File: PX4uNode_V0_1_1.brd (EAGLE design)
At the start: 45.4 x 34 mm, 129 parts, among them M3_MOUNT1101 MOUNT-HOLE3.1MM, M3_MOUNT1102 MOUNT-HOLE3.1MM, M3_MOUNT1103 MOUNT-HOLE3.1MM, M3_MOUNT1104 MOUNT-HOLE3.1MM, U101 STM32F4X7VX, U401 MAX3051, U402 MAX3051, X101 3.2x2.5 mm / 24 MHz / 15 ppm

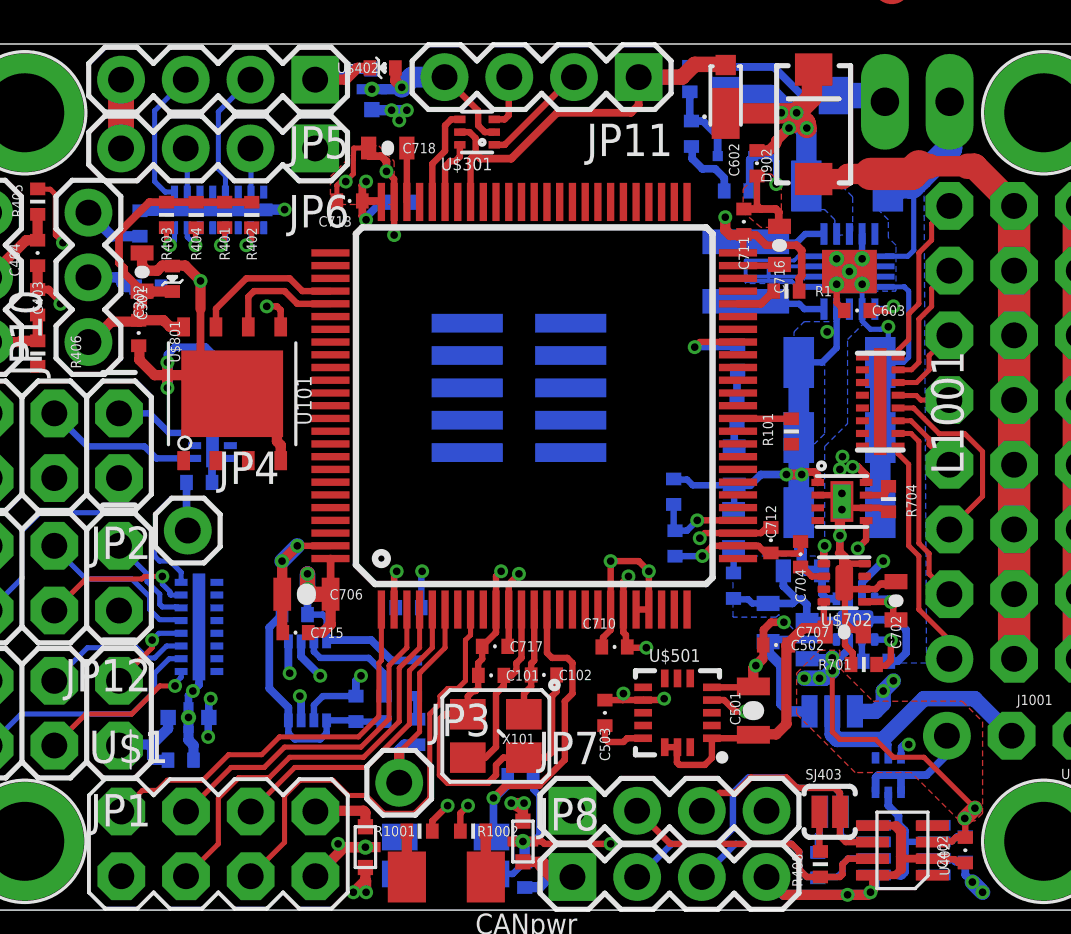
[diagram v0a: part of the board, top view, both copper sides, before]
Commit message: Battery added.  Floods added to power tracks
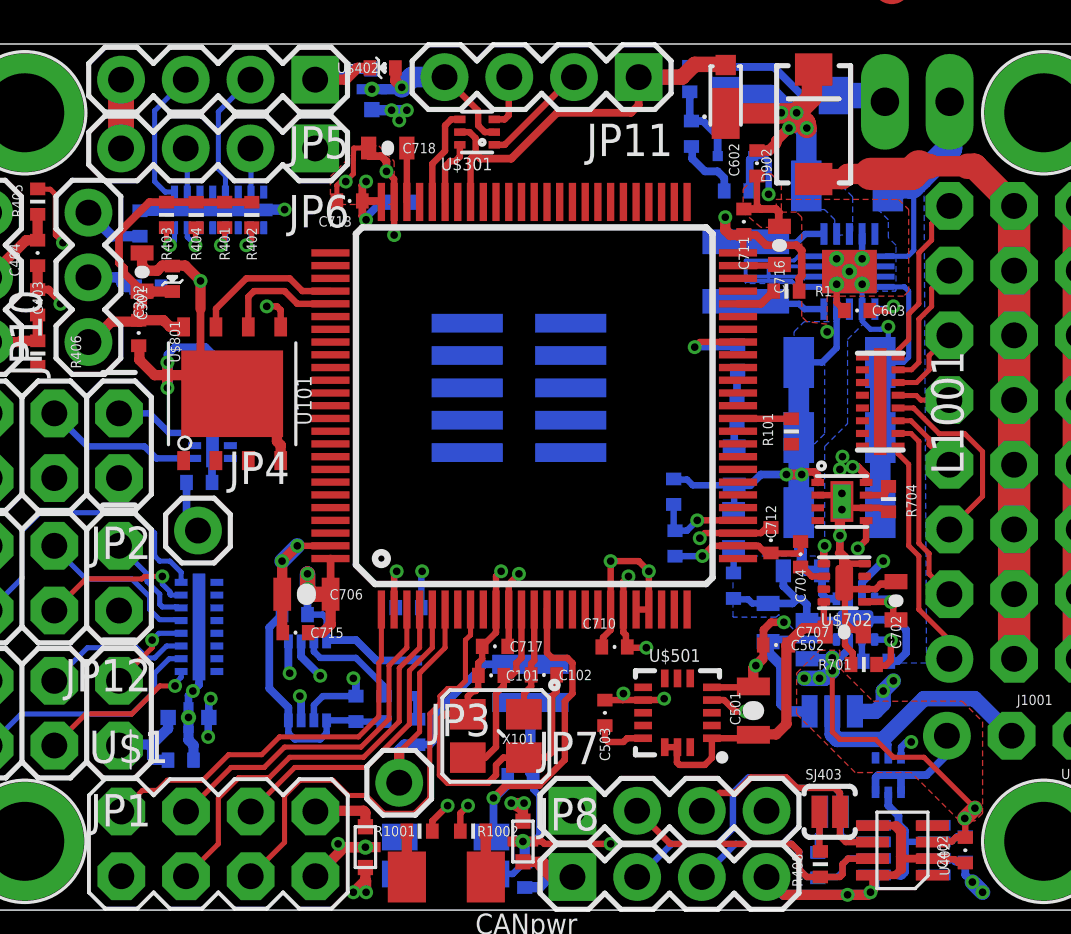
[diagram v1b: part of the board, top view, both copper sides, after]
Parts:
- added U$4: MS621FE, pixhawk2:MS621FE
- moved JP4 0.40 mm to (22.3, 19.1)
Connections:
- net GND: now also U$4.2
- net VBAT: now also U$4.1
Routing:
- net VBAT: track 9.65 -> 16.0 mm
- net GND: track 233.2 -> 236.3 mm
- added copper zone on layer 15, net 5V_S3_FILTERED
- added copper zone on layer 15, net VDD_5V_PERIPH

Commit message: Almost routed
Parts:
- moved R101 0.40 mm to (45.6, 22.6)
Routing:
- net FMU-CH8: track 0.97 -> 47.3 mm, vias 1 -> 7
- net CAN1_TX: track 0.00 -> 45.7 mm, vias 0 -> 3
- net FMU_AUX_ADC1: track 2.80 -> 47.7 mm, vias 1 -> 6
- net CAN1_RX: track 0.00 -> 44.5 mm, vias 0 -> 6
- net SPEKTRUM_RX: track 0.91 -> 40.3 mm, vias 1 -> 6
- net CAN2_TX: track 0.00 -> 38.7 mm, vias 0 -> 6
- net FMU-USART3_RTS: track 0.00 -> 37.7 mm, vias 0 -> 3
- net CAN2_RX: track 0.00 -> 37.6 mm, vias 0 -> 4
- net FMU-USART3_RX: track 0.00 -> 36.1 mm, vias 0 -> 5
- net !VDD_5V_PERIPH_EN: track 1.23 -> 37.1 mm, vias 1 -> 6
- net FMU-USART3_CTS: track 0.00 -> 34.9 mm, vias 0 -> 6
- net ACCEL_DRDY: track 0.00 -> 34.1 mm, vias 0 -> 2
- net FMU_AUX_ADC2: track 0.00 -> 31.3 mm, vias 0 -> 2
- net FMU-LED_SAFETY: track 0.00 -> 30.4 mm, vias 0 -> 4
- net FMU-USART3_TX: track 0.00 -> 30.3 mm, vias 0 -> 5
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
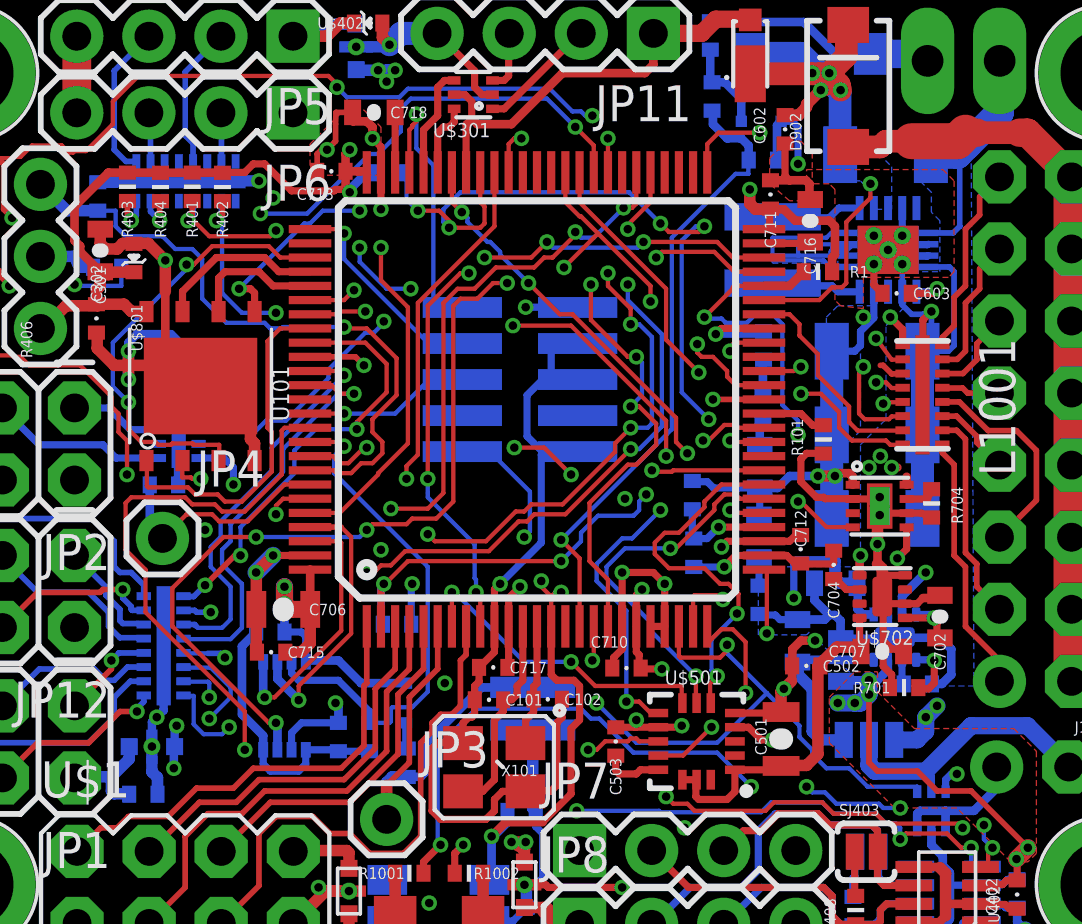
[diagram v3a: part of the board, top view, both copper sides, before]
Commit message: Servo output channels ripped up for reshuffle
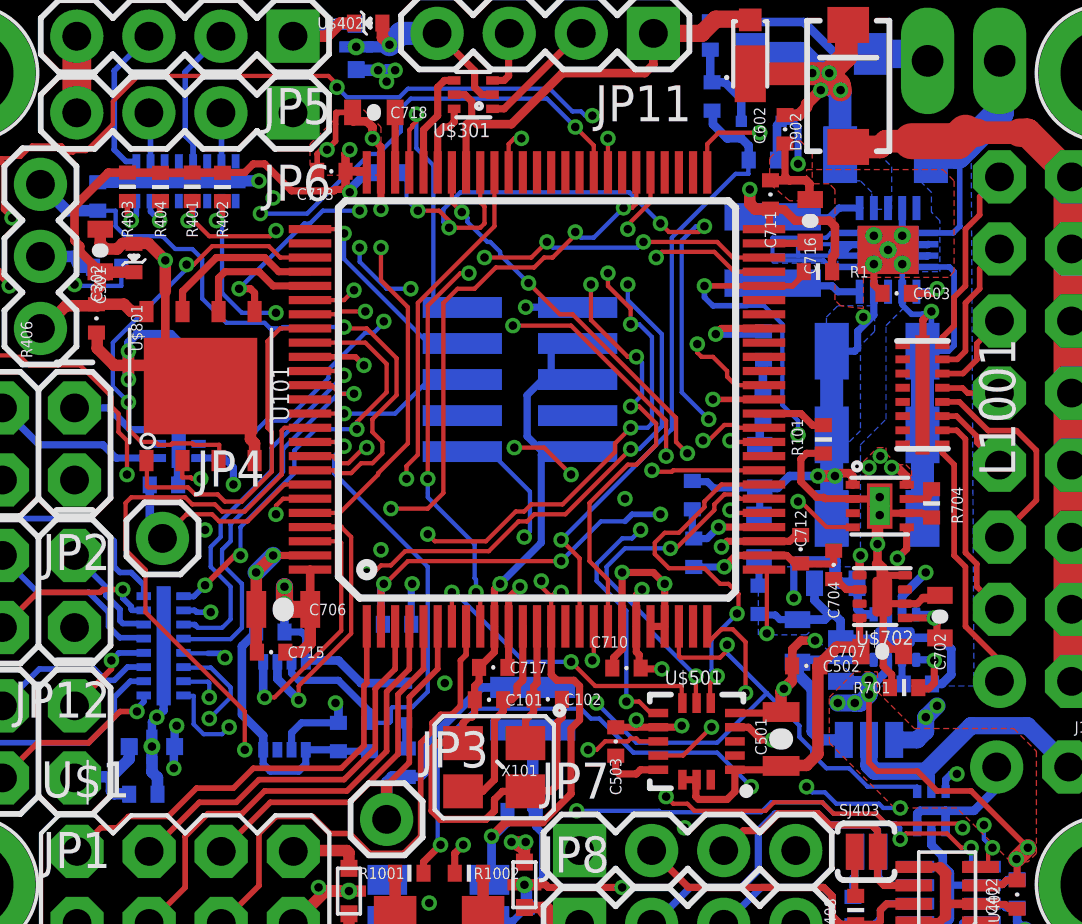
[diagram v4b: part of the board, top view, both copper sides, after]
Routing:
- net FMU-CH8: track 47.3 -> 0.04 mm, vias 7 -> 0
- net FMU-CH1: track 20.1 -> 0.00 mm, vias 2 -> 0
- net FMU-CH5: track 17.0 -> 0.00 mm, vias 2 -> 0
- net FMU-CH7: track 15.7 -> 0.00 mm, vias 2 -> 0
- net FMU-CH3: track 9.97 -> 0.00 mm, vias 2 -> 0
- net FMU-CH2: track 7.58 -> 0.00 mm
- net FMU-CH4: track 7.10 -> 0.21 mm, vias 2 -> 0
- net SPI_INT_SCK: track 16.4 -> 12.1 mm
- net FMU-CH6: track 0.91 -> 0.00 mm
- added copper zone on layer 1, net VDD_5V_PERIPH

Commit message: Layout done
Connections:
- net FMU-CH1: now also L1001.P$4; no longer L1001.P$8
- net FMU-CH2: now also L1001.P$5; no longer L1001.P$7
- net FMU-CH3: now also L1001.P$6; no longer L1001.P$5
- net FMU-CH4: now also L1001.P$7; no longer L1001.P$6
- net FMU-CH5: now also L1001.P$2; no longer L1001.P$4
- net FMU-CH7: now also L1001.P$8; no longer L1001.P$2
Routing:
- net FMU-CH8: track 0.04 -> 42.0 mm, vias 0 -> 5
- net FMU-CH6: track 0.00 -> 21.4 mm, vias 0 -> 3
- net FMU-CH7: track 0.00 -> 15.7 mm, vias 0 -> 2
- net FMU-CH5: track 0.00 -> 15.3 mm, vias 0 -> 2
- net FMU-CH1: track 0.00 -> 6.63 mm
- net FMU-CH2: track 0.00 -> 6.46 mm
- net FMU-CH3: track 0.00 -> 6.00 mm
- net FMU-CH4: track 0.21 -> 5.96 mm
- net VDD_5V_PERIPH: track 86.8 -> 91.3 mm
- net CAN1_RX: track 44.5 -> 46.3 mm
- net FMU-USART3_CTS: track 34.9 -> 33.9 mm, vias 6 -> 4
- net !GYRO_CS: track 11.3 -> 12.2 mm
- net SPEKTRUM_RX: track 40.3 -> 41.2 mm
- net MAG_DRDY: track 15.6 -> 16.3 mm
- net !VDD_5V_PERIPH_OC: track 16.1 -> 16.8 mm
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
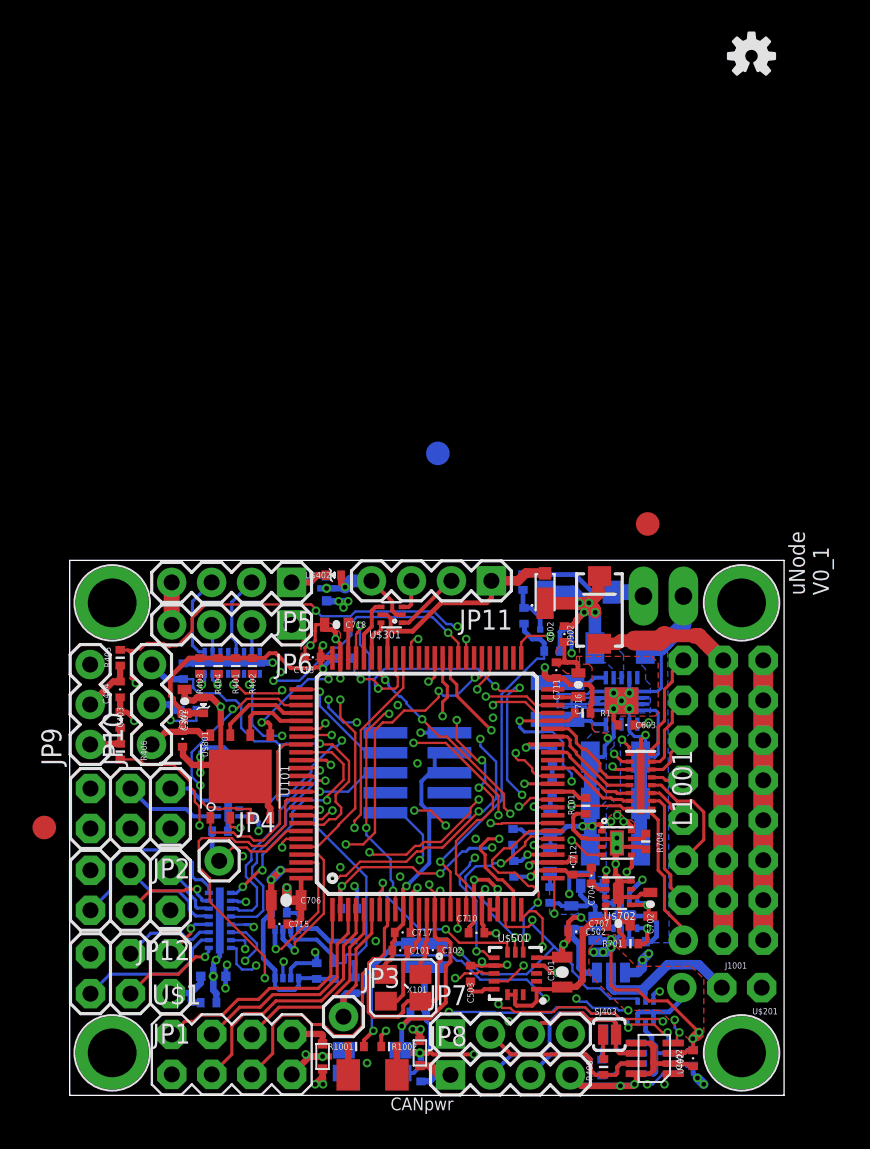
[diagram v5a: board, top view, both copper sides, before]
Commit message: Much trace tidying and simplification
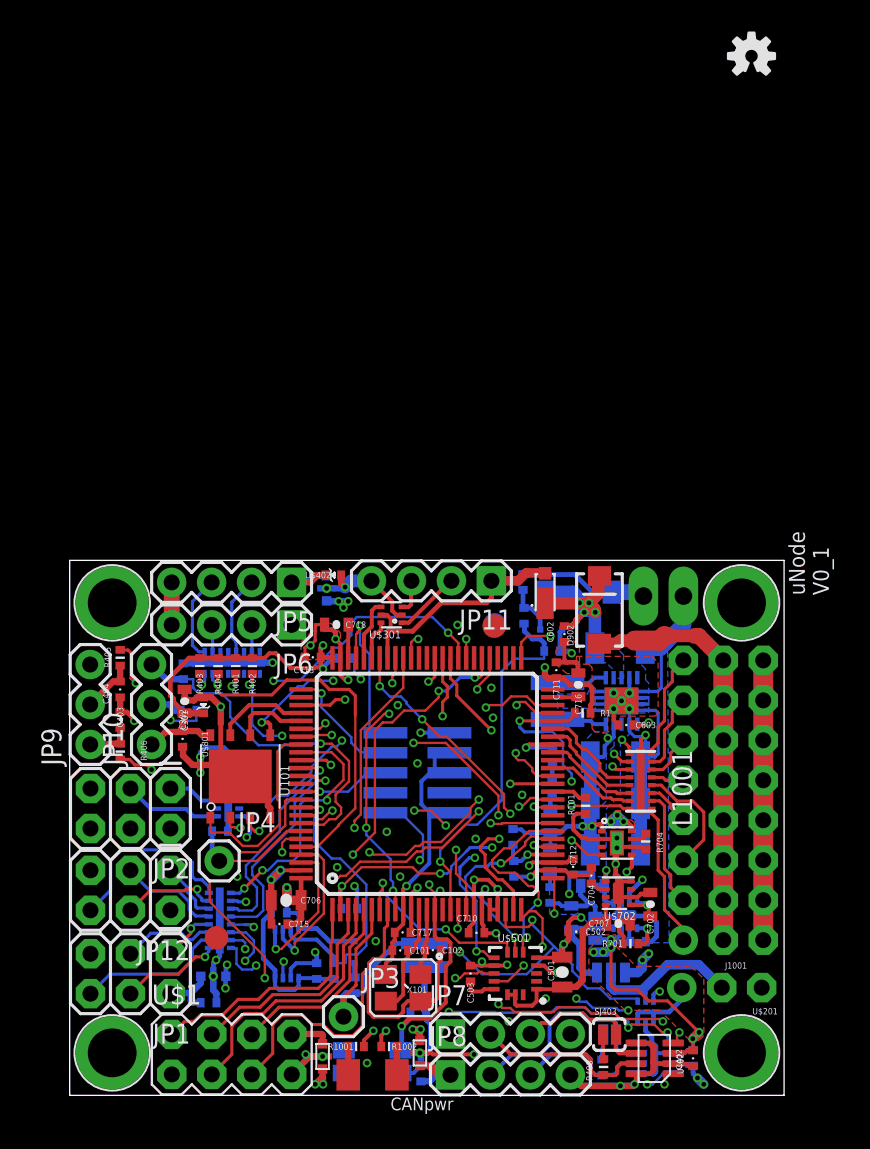
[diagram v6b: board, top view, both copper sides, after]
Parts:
- moved JP1103 38.0 mm to (22.1, 14.2)
- moved JP1104 31.3 mm to (39.8, 34.0)
- moved JP1102 11.5 mm to (39.8, 34.1)
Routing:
- net GND: track 266.0 -> 251.8 mm
- net SDIO_D2: track 15.9 -> 22.4 mm, vias 2 -> 3
- net FMU_AUX_ADC1: track 47.7 -> 43.8 mm, vias 6 -> 3
- net !VDD_5V_PERIPH_EN: track 37.1 -> 33.3 mm, vias 6 -> 5
- net FMU-CH9: track 24.9 -> 21.2 mm
- net VDD_IN: track 14.1 -> 16.3 mm
- net VDD_5V_PERIPH: track 91.3 -> 93.2 mm
- net VDD_SERVO_SENSE: track 22.3 -> 23.6 mm
- net FMU-USART3_RX: track 36.2 -> 34.9 mm
- net FMU-UART7_RX: track 22.8 -> 23.8 mm
- net FMU_AUX_ADC2: track 31.3 -> 30.4 mm
- net FMU-USART2_CTS: track 15.4 -> 16.2 mm
- net FMU-I2C1_SDA: track 22.6 -> 23.2 mm, vias 3 -> 1
- net FMU-I2C1_SCL: track 15.3 -> 15.9 mm
- net FMU-USART3_TX: track 30.3 -> 29.9 mm, vias 5 -> 4
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
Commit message: More layout cleanup done
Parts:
- moved JP1104 0.39 mm to (40.0, 34.3)
- moved JP1102 0.28 mm to (40.0, 34.3)
- moved R707 0.15 mm to (41.1, 20.6)
- moved R708 0.11 mm to (41.1, 18.5)
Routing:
- net FMU-USART3_RX: track 34.9 -> 44.8 mm, vias 5 -> 3
- net SPEKTRUM_RX: track 41.5 -> 46.9 mm
- net GND: track 251.8 -> 247.6 mm, vias 27 -> 29
- net CAN2_RX: track 37.6 -> 34.1 mm
- net FMU-CH8: track 42.0 -> 43.6 mm
- net CAN1_RX: track 46.7 -> 45.4 mm
- net FMU-LED_SAFETY: track 30.4 -> 29.3 mm, vias 4 -> 3
- net CAN2_TX: track 38.7 -> 38.0 mm, vias 6 -> 4
- net CAN1_TX: track 45.7 -> 45.2 mm
- net FMU-!RESET: track 37.4 -> 37.0 mm, vias 5 -> 3
